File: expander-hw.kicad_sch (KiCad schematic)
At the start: 29 parts, among them J1 Conn_ARM_JTAG_SWD_10, J2 USB_C_Receptacle_USB2.0_16P, J3 Conn_02x08_Odd_Even, U1 STM32U545RETxQ, U2 USBLC6-2SC6, U3 AZ1117-3.3, U4 SRDA3.3-4BTG, U5 SRDA3.3-4BTG, U6 SRDA3.3-4BTG, X1 ECS-2520MV-xxx-xx

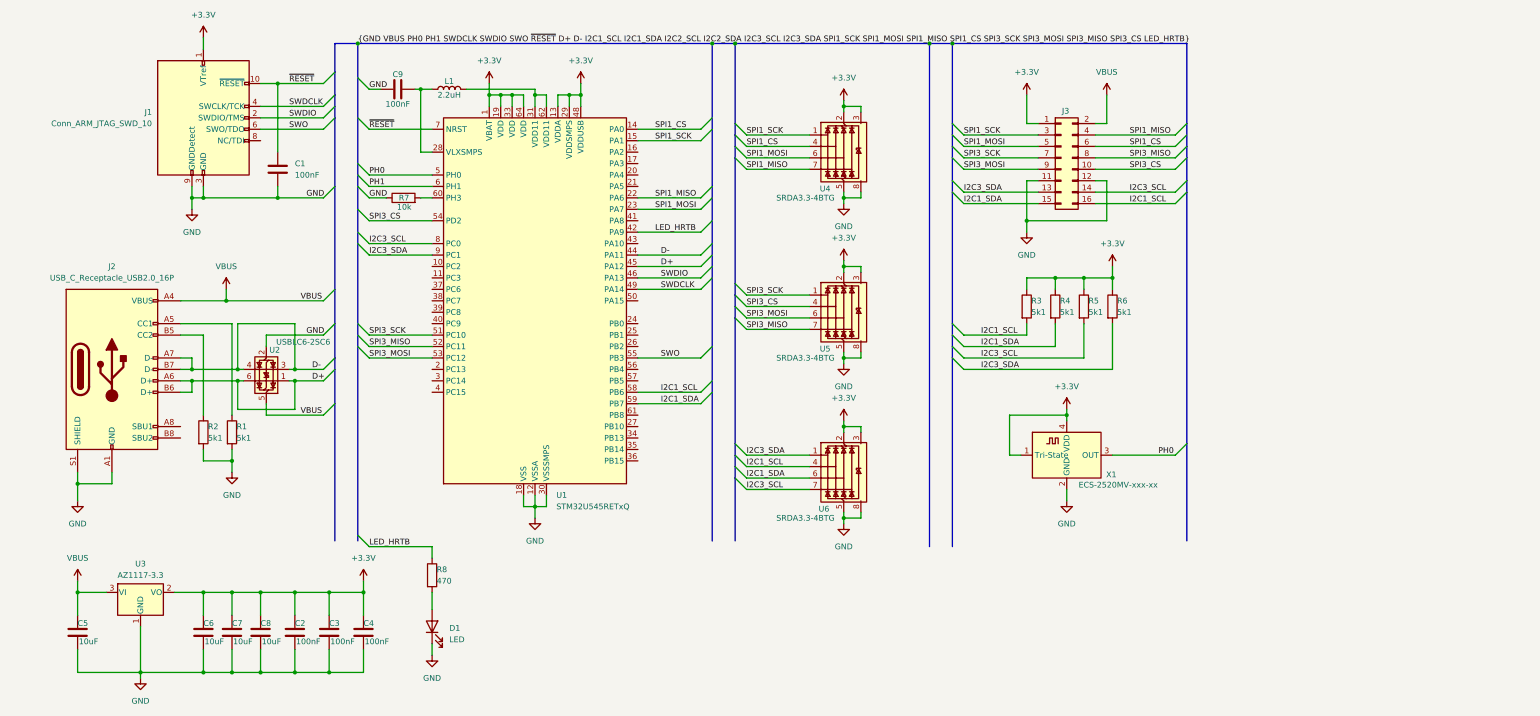
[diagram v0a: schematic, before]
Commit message: Fix SMPS, remove XTAL
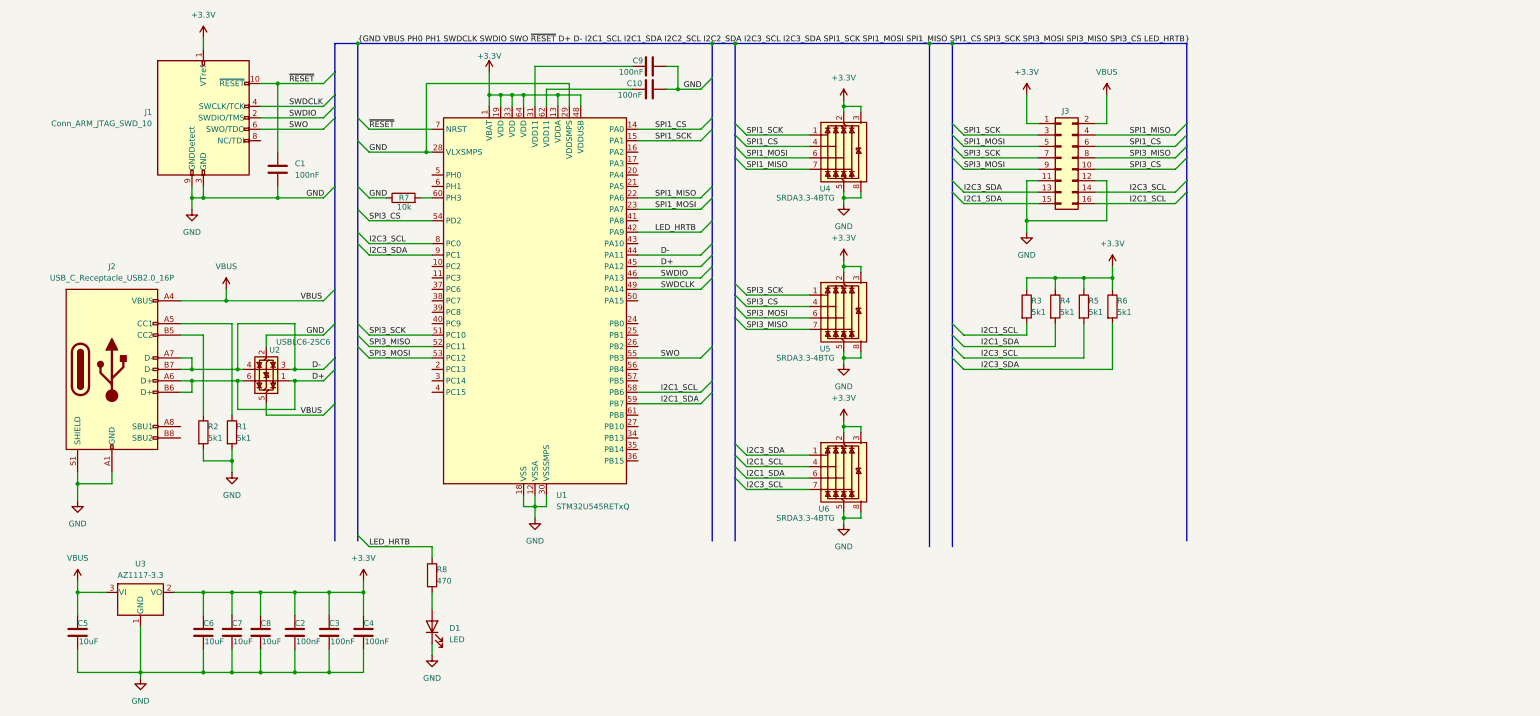
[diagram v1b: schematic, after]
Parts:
- removed L1: 2.2uH, Inductor_SMD:L_0805_2012Metric, symbol Device:L
- removed X1: ECS-2520MV-xxx-xx, Crystal:Crystal_SMD_TXC_7M-4Pin_3.2x2.5mm, symbol Oscillator:ECS-2520MV-xxx-xx
- added C10: 100nF, Capacitor_SMD:C_0603_1608Metric, symbol Device:C
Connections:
- net +3.3V: no longer U1.29 (VDDSMPS)
- net GND: now also U1.28 (VLXSMPS), U1.29 (VDDSMPS), C10.1
- net at C9.2: now also U1.31 (VDD11); no longer U1.28 (VLXSMPS)
- net at U1.62 (VDD11): now also C10.2; no longer U1.31 (VDD11)
- net PH0: no longer names the net of U1.5 (PH0)
- net PH1: no longer names the net of U1.6 (PH1)
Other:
- moved on the sheet: C9

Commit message: Add HW version + boot test point + SWD tag connector
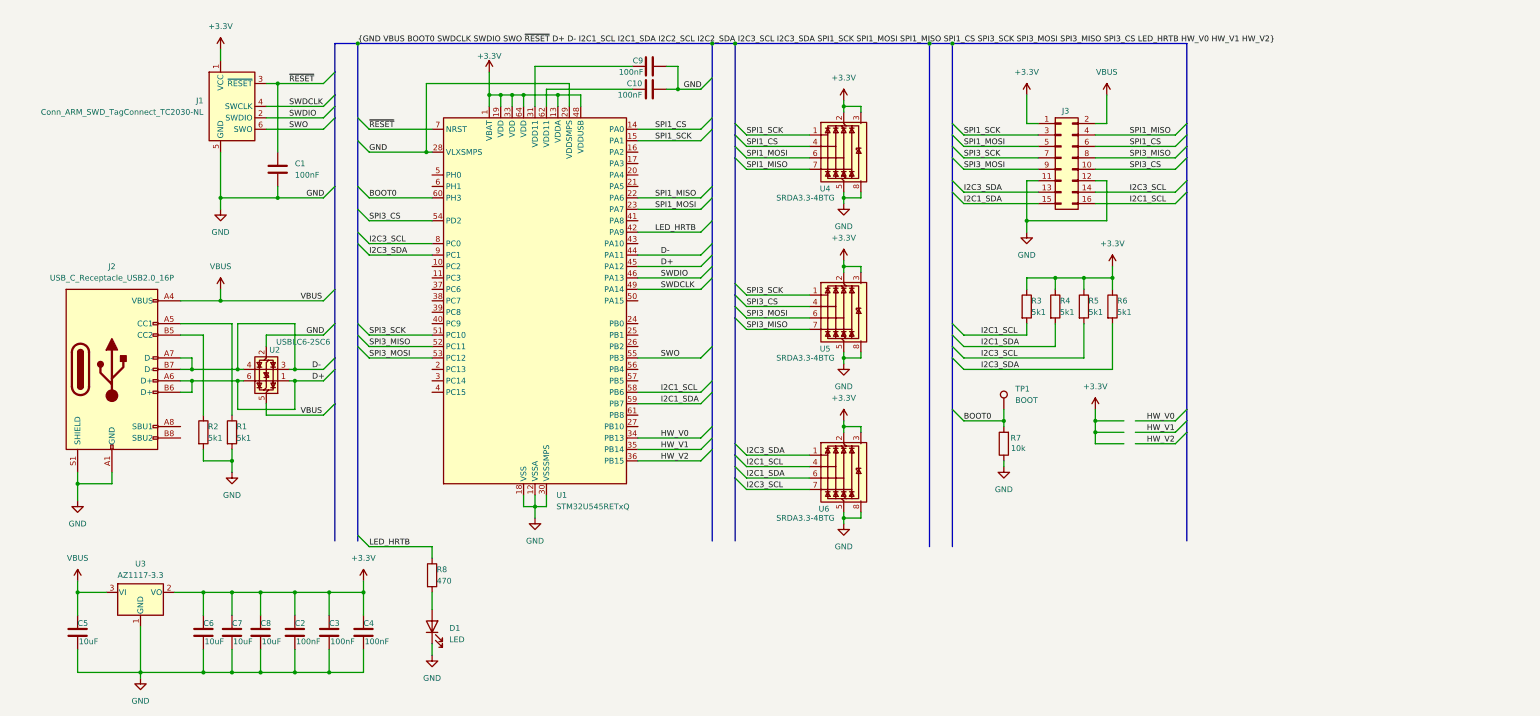
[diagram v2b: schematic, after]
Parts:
- removed J1: Conn_ARM_JTAG_SWD_10, Connector_PinHeader_1.27mm:PinHeader_2x05_P1.27mm_Vertical, symbol Connector:Conn_ARM_JTAG_SWD_10
- added J1: Conn_ARM_SWD_TagConnect_TC2030-NL, Connector:Tag-Connect_TC2030-IDC-NL_2x03_P1.27mm_Vertical, symbol Connector:Conn_ARM_SWD_TagConnect_TC2030-NL
- added TP1: BOOT, TestPoint:TestPoint_Pad_D1.0mm, symbol Connector:TestPoint
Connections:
- net +3.3V: now also J1.1 (VCC)
- net GND: now also J1.5 (GND)
- net SWDCLK: now also J1.4 (SWCLK)
- net SWDIO: now also J1.2 (SWDIO)
- net SWO: now also J1.6 (SWO)
- net ~{RESET}: now also J1.3 (~{RESET})
- net HW_V0: now reaches U1.34 (PB13)
- net HW_V1: now reaches U1.35 (PB14)
- net HW_V2: now reaches U1.36 (PB15)
- net BOOT0: now reaches R7.2, U1.60 (PH3)
- net BOOT0: now also TP1.1
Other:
- moved on the sheet: R7

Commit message: Switch to stm32h523 mcu
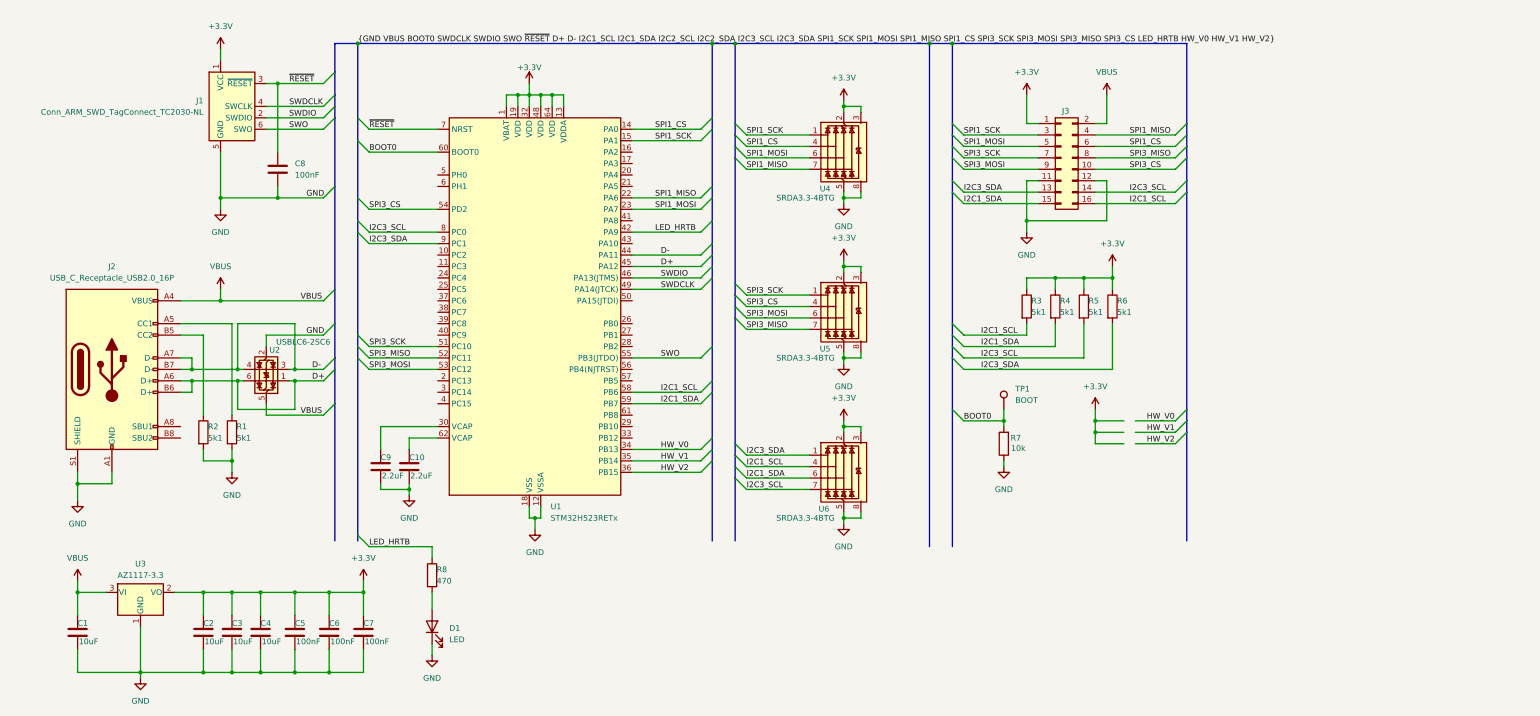
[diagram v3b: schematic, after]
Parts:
- removed U1: STM32U545RETxQ, Package_QFP:LQFP-64_10x10mm_P0.5mm, symbol MCU_ST_STM32U5:STM32U545RETxQ
- added U1: STM32H523RETx, Package_QFP:LQFP-64_10x10mm_P0.5mm, symbol expander-hw:STM32H523RETx
- C10, C9: value 100nF -> 2.2uF
- renumbered C5 to C1, C6 to C2, C7 to C3, C8 to C4, C2 to C5, C3 to C6, C4 to C7, C1 to C8
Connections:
- net +3.3V: now also U1.1 (VBAT), U1.13 (VDDA), U1.19 (VDD), U1.32 (VDD), U1.48 (VDD), U1.64 (VDD)
- net BOOT0: now also U1.60 (BOOT0)
- net D+: now also U1.45 (PA12)
- net D-: now also U1.44 (PA11)
- net GND: now also C10.2, C9.2, U1.12 (VSSA), U1.18 (VSS), U1.31 (VSS), U1.47 (VSS), U1.63 (VSS); no longer C10.1, C9.1
- net HW_V0: now also U1.34 (PB13)
- net HW_V1: now also U1.35 (PB14)
- net HW_V2: now also U1.36 (PB15)
- net I2C1_SCL: now also U1.58 (PB6)
- net I2C1_SDA: now also U1.59 (PB7)
- net I2C3_SCL: now also U1.8 (PC0)
- net I2C3_SDA: now also U1.9 (PC1)
- net LED_HRTB: now also U1.42 (PA9)
- net SPI1_CS: now also U1.14 (PA0)
- net SPI1_MISO: now also U1.22 (PA6)
- net SPI1_MOSI: now also U1.23 (PA7)
- net SPI1_SCK: now also U1.15 (PA1)
- net SPI3_CS: now also U1.54 (PD2)
- net SPI3_MISO: now also U1.52 (PC11)
- net SPI3_MOSI: now also U1.53 (PC12)
- net SPI3_SCK: now also U1.51 (PC10)
- net SWDCLK: now also U1.49 (PA14(JTCK))
- net SWDIO: now also U1.46 (PA13(JTMS))
- net SWO: now also U1.55 (PB3(JTDO))
- net ~{RESET}: now also U1.7 (NRST)
- new net: C9.1, U1.30 (VCAP)
- new net: C10.1, U1.62 (VCAP)

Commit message: Fix stm32h523 pinout
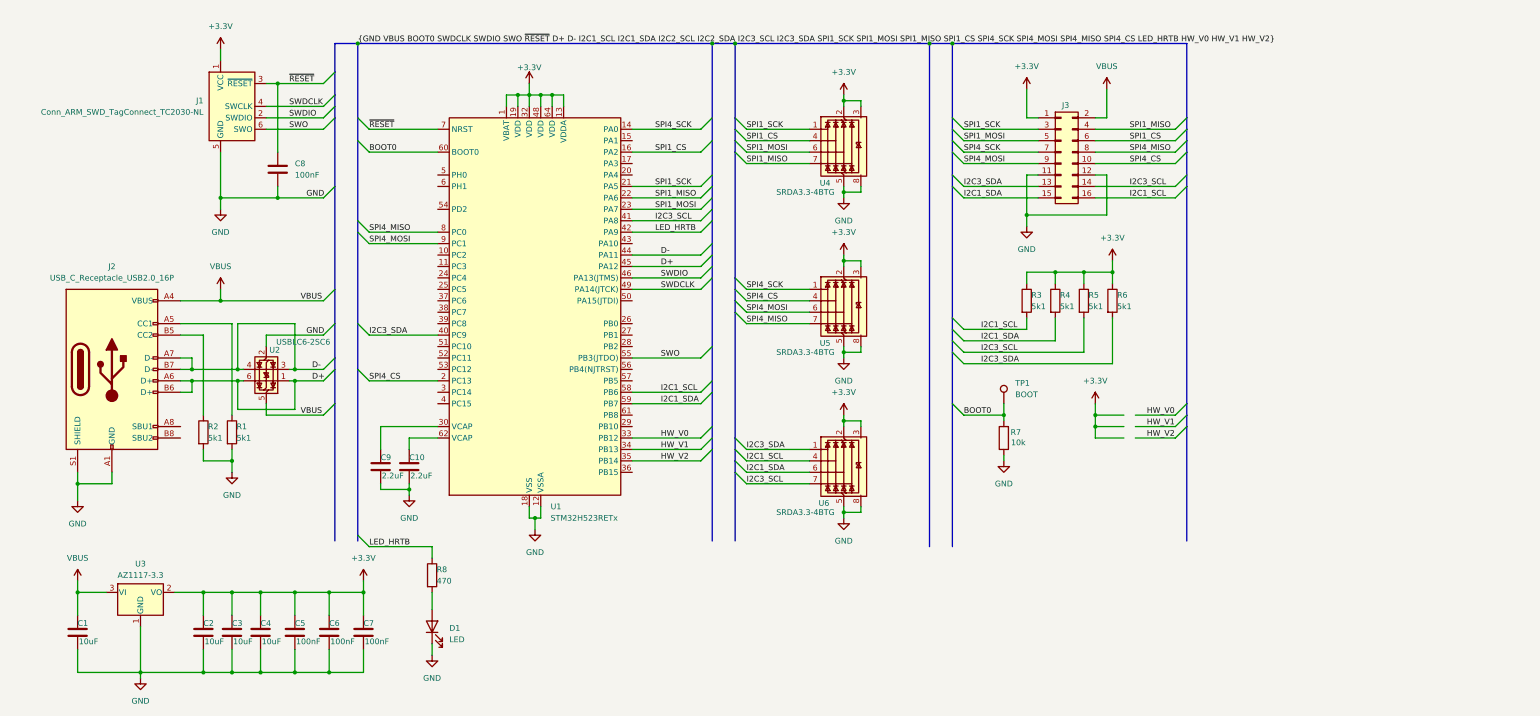
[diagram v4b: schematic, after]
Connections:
- net HW_V0: now also U1.33 (PB12); no longer U1.34 (PB13)
- net HW_V1: now also U1.34 (PB13); no longer U1.35 (PB14)
- net HW_V2: now also U1.35 (PB14); no longer U1.36 (PB15)
- net I2C3_SCL: now also U1.41 (PA8); no longer U1.8 (PC0)
- net I2C3_SDA: now also U1.40 (PC9); no longer U1.9 (PC1)
- net SPI1_CS: now also U1.16 (PA2); no longer U1.14 (PA0)
- net SPI1_SCK: now also U1.21 (PA5); no longer U1.15 (PA1)
- net SPI4_CS: now reaches U1.2 (PC13)
- net SPI4_CS: now also J3.10 (Pin_10), U5.4 (I/O2)
- removed net SPI3_CS: J3.10 (Pin_10), U1.54 (PD2), U5.4 (I/O2)
- net SPI3_MISO renamed SPI4_MISO
- net SPI4_MISO: now also U1.8 (PC0); no longer U1.52 (PC11)
- net SPI3_MOSI renamed SPI4_MOSI
- net SPI4_MOSI: now also U1.9 (PC1); no longer U1.53 (PC12)
- net SPI3_SCK renamed SPI4_SCK
- net SPI4_SCK: now also U1.14 (PA0); no longer U1.51 (PC10)
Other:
- moved on the sheet: J3, R3, R4, R5, R6, R7, TP1, U4, U5, U6
